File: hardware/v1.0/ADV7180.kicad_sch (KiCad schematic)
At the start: 47 parts, among them J5 Conn_01x03, J6 Conn_01x03, J7 Conn_01x04, J8 Conn_01x34, U13 TLV75718PDRV, U2 CH32V003JxMx, U4 ADV7180BCP32Z-RL, U5 TLV62568DRL, Y1 28.63636MHz

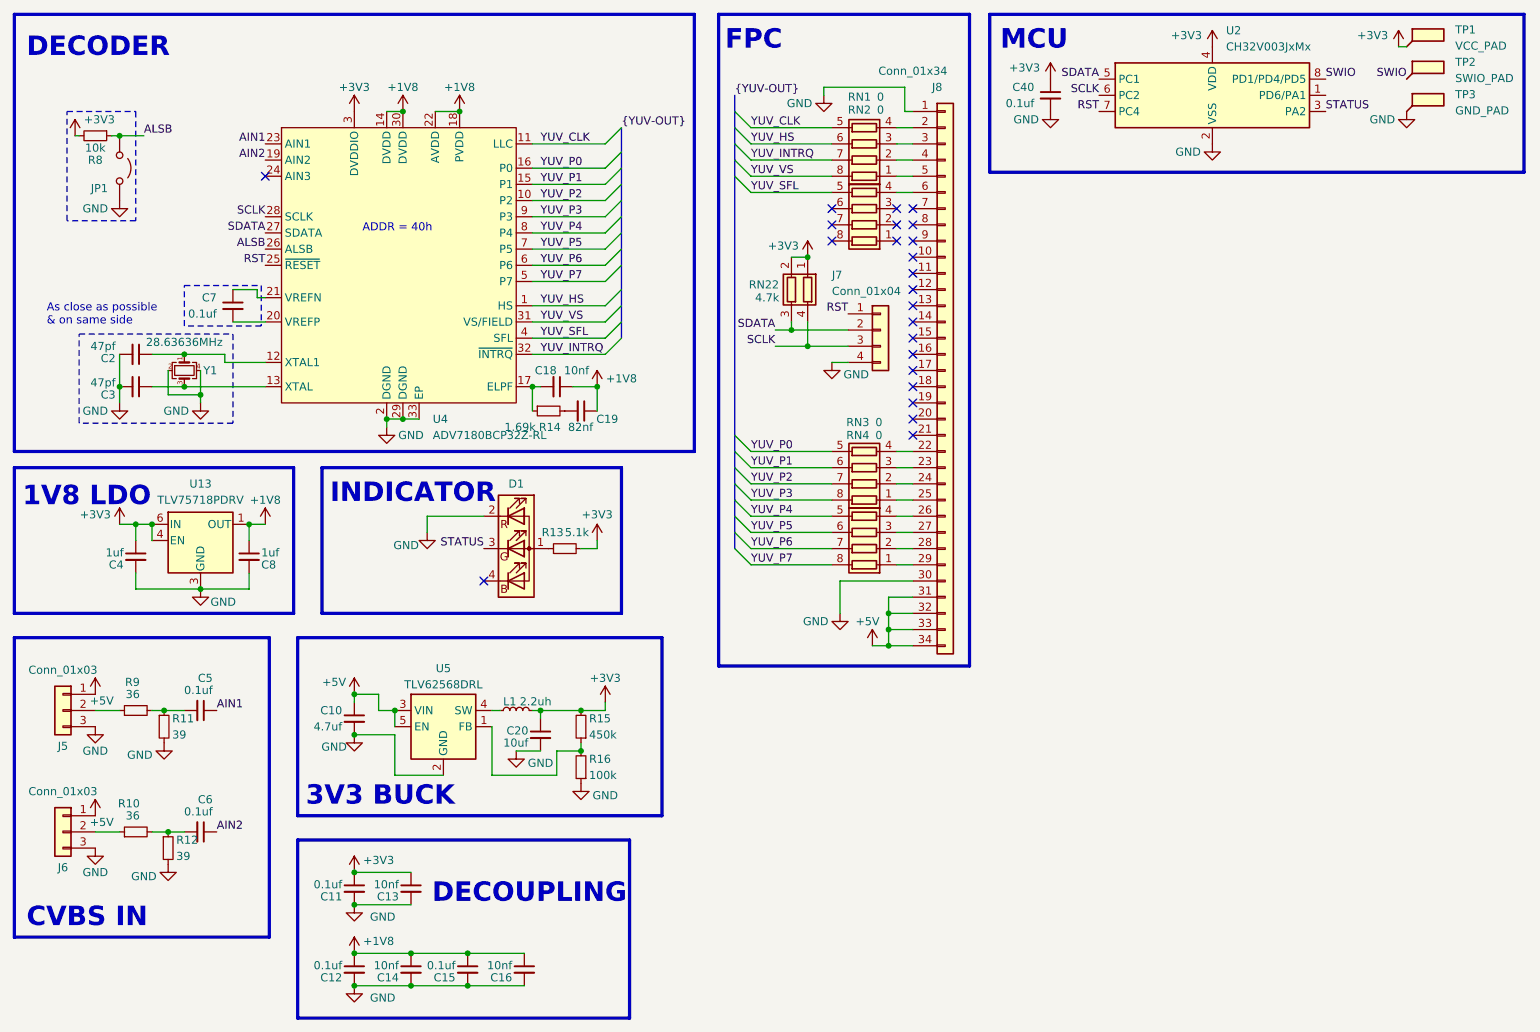
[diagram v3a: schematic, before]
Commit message: added tvs diode+changed inductors
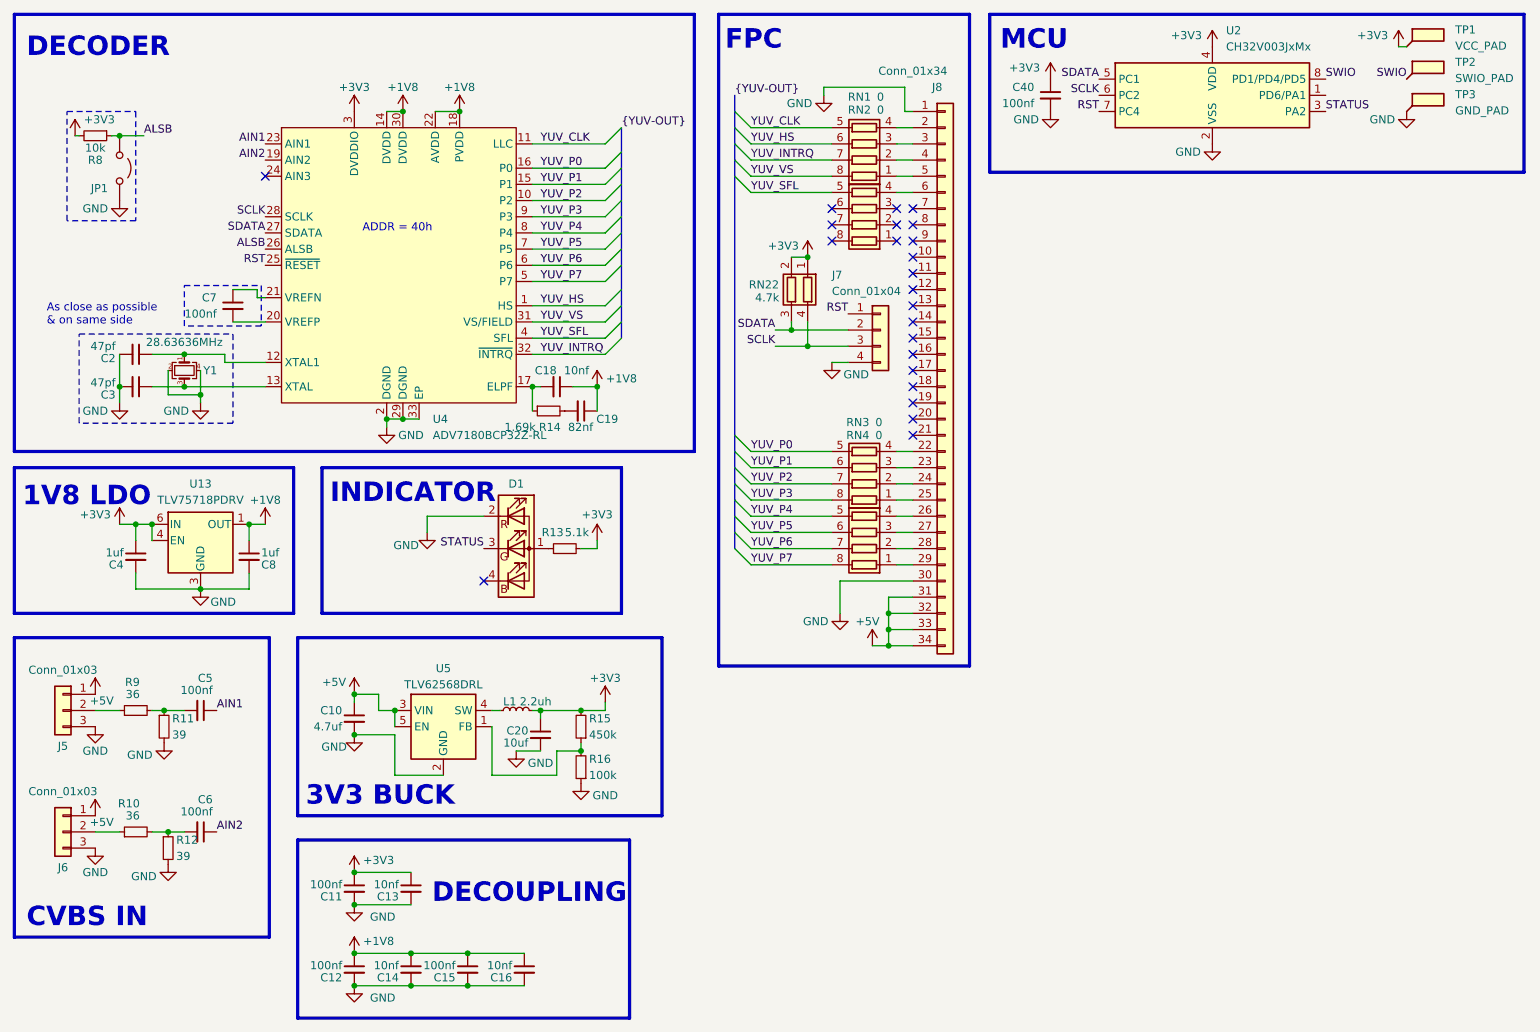
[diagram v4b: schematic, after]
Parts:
- C11, C12, C15, C40, C5, C6, C7: value 0.1uf -> 100nf
- L1: footprint Inductor_SMD:L_0603_1608Metric -> Inductor_SMD:L_0805_2012Metric
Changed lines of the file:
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@@
 			)
 		)
-		(property "Value" "0.1uf"
+		(property "Value" "100nf"
 			(at 46.355 140.335 90)
 			(effects
@@
 			)
 		)
-		(property "Value" "0.1uf"
+		(property "Value" "100nf"
 			(at 46.355 121.285 90)
 			(effects
@@
 			)
 		)
-		(property "Value" "0.1uf"
+		(property "Value" "100nf"
 			(at 66.675 164.465 0)
 			(effects
@@
 			)
 		)
-		(property "Value" "0.1uf"
+		(property "Value" "100nf"
 			(at 175.26 29.21 0)
 			(effects
@@
 			)
 		)
-		(property "Value" "0.1uf"
+		(property "Value" "100nf"
 			(at 84.455 164.465 0)
 			(effects
@@
 			)
 		)
-		(property "Value" "0.1uf"
+		(property "Value" "100nf"
 			(at 66.675 151.765 0)
 			(effects
@@
 			)
 		)
-		(property "Footprint" "Inductor_SMD:L_0603_1608Metric"
+		(property "Footprint" "Inductor_SMD:L_0805_2012Metric"
 			(at 93.98 124.46 0)
 			(effects
@@
 			)
 		)
-		(property "Value" "0.1uf"
+		(property "Value" "100nf"
 			(at 46.99 62.23 0)
 			(effects
